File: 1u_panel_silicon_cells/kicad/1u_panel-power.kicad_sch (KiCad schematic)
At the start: 70 parts, among them J1 MMS-104-01-[F/L]-SH, Q1 DMP3050LVT-7, Q2 DMP2240UDM-7, U10 TPS63060DSCR, U12 LTC4412, U3 LT1618EMSTRPBF, U4 INA226

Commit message: Updated all PN/DS/DPN/MPN/etc. for silicon solar module components
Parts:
- C12: DPN 490-12379-1-ND -> 490-10516-2-ND; MPN GRT21BR61C106KE01L -> GRM21BR71A106KA73L
- C14, C18: DPN 587-4332-1-ND -> 490-GRM188Z71C475KE21JTR-ND; MFR Taiyo -> Murata; MPN EMK107BBJ475KAHT -> GRM188Z71C475KE21J
- C2: DPN 587-5957-1-ND -> 490-4781-2-ND; MFR Taiyo -> Murata; MPN UMK107B7103KAHT -> GCM188R72A103KA37D
- C21, C6, C7, C8: DPN 1276-6985-1-ND -> 490-5798-2-ND; MFR Kemet -> Murata; MPN CL10B104KB85PND -> GCJ188R71H104KA12D
- C22: DPN 490-12317-1-ND -> 490-8011-2-ND; MPN GRT188R61C106KE13D -> GCM1885G1H100JA16D
- L1: DPN 445-VLS3010CX-1R5M-1CT-ND -> 490-14149-2-ND; MFR TDK -> Murata
- R1: DPN A129720CT-ND -> YAG4574TR-ND; MFR TE -> Yaego; MPN CRGCQ0603F470K -> RT0603BRD07560KL
- R17: DPN 541-100MAHTR-ND -> P19308TR-ND; MFR Vishay -> Panasonic; MPN CRCW0603100MJPEAHR -> ERJ-6DSFR10V
- R18, R19, R6, R7: DPN RNCP0603FTD10K0CT-ND -> RR08P100KDCT-ND; MFR Stackpole -> Susumu; MPN RNCP0603FTD10K0 -> RR0816P-104-D
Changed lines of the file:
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@@
 			)
 		)
-		(property "DPN" "1276-6985-1-ND"
+		(property "DPN" "490-5798-2-ND"
 			(at 118.11 77.47 0)
 			(effects
@@
 			)
 		)
-		(property "MFR" "Kemet"
+		(property "MFR" "Murata"
 			(at 118.11 77.47 0)
 			(effects
@@
 			)
 		)
-		(property "MPN" "CL10B104KB85PND"
+		(property "MPN" "GCJ188R71H104KA12D"
 			(at 118.11 77.47 0)
 			(effects
@@
 			)
 		)
-		(property "DPN" "587-5957-1-ND"
+		(property "DPN" "490-4781-2-ND"
 			(at 223.52 105.41 0)
 			(effects
@@
 			)
 		)
-		(property "MFR" "Taiyo"
+		(property "MFR" "Murata"
 			(at 223.52 105.41 0)
 			(effects
@@
 			)
 		)
-		(property "MPN" "UMK107B7103KAHT"
+		(property "MPN" "GCM188R72A103KA37D"
 			(at 223.52 105.41 0)
 			(effects
@@
 			)
 		)
-		(property "DPN" "445-VLS3010CX-1R5M-1CT-ND"
+		(property "DPN" "490-14149-2-ND"
 			(at 182.88 205.74 0)
 			(effects
@@
 			)
 		)
-		(property "MFR" "TDK"
+		(property "MFR" "Murata"
 			(at 182.88 205.74 0)
 			(effects
@@
 			)
 		)
-		(property "DPN" "587-4332-1-ND"
+		(property "DPN" "490-GRM188Z71C475KE21JTR-ND"
 			(at 238.76 64.77 0)
 			(effects
@@
 			)
 		)
-		(property "MFR" "Taiyo"
+		(property "MFR" "Murata"
 			(at 238.76 64.77 0)
 			(effects
@@
 			)
 		)
-		(property "MPN" "EMK107BBJ475KAHT"
+		(property "MPN" "GRM188Z71C475KE21J"
 			(at 238.76 64.77 0)
 			(effects
@@
 			)
 		)
-		(property "DPN" "A129720CT-ND"
+		(property "DPN" "YAG4574TR-ND"
 			(at 219.71 198.12 0)
 			(effects
@@
 			)
 		)
-		(property "MFR" "TE"
+		(property "MFR" "Yaego"
 			(at 219.71 198.12 0)
 			(effects
@@
 			)
 		)
-		(property "MPN" "CRGCQ0603F470K"
+		(property "MPN" "RT0603BRD07560KL"
 			(at 219.71 198.12 0)
 			(effects
@@
 			)
 		)
-		(property "DPN" "RNCP0603FTD10K0CT-ND"
+		(property "DPN" "RR08P100KDCT-ND"
 			(at 162.56 100.33 0)
 			(effects
@@
 			)
 		)
-		(property "MFR" "Stackpole"
+		(property "MFR" "Susumu"
 			(at 162.56 100.33 0)
 			(effects
@@
 			)
 		)
-		(property "MPN" "RNCP0603FTD10K0"
+		(property "MPN" "RR0816P-104-D"
 			(at 162.56 100.33 0)
 			(effects
@@
 			)
 		)
-		(property "DPN" "RNCP0603FTD10K0CT-ND"
+		(property "DPN" "RR08P100KDCT-ND"
 			(at 177.8 104.14 0)
 			(effects
@@
 			)
 		)
-		(property "MFR" "Stackpole"
+		(property "MFR" "Susumu"
 			(at 177.8 104.14 0)
 			(effects
@@
 			)
 		)
-		(property "MPN" "RNCP0603FTD10K0"
+		(property "MPN" "RR0816P-104-D"
 			(at 177.8 104.14 0)
 			(effects
@@
 			)
 		)
-		(property "DPN" "RNCP0603FTD10K0CT-ND"
+		(property "DPN" "RR08P100KDCT-ND"
 			(at 290.83 86.36 0)
 			(effects
@@
 			)
 		)
-		(property "MFR" "Stackpole"
+		(property "MFR" "Susumu"
 			(at 290.83 86.36 0)
 			(effects
@@
 			)
 		)
-		(property "MPN" "RNCP0603FTD10K0"
+		(property "MPN" "RR0816P-104-D"
 			(at 290.83 86.36 0)
 			(effects
@@
 			)
 		)
-		(property "DPN" "1276-6985-1-ND"
+		(property "DPN" "490-5798-2-ND"
 			(at 208.28 222.25 0)
 			(effects
@@
 			)
 		)
-		(property "MFR" "Kemet"
+		(property "MFR" "Murata"
 			(at 208.28 222.25 0)
 			(effects
@@
 			)
 		)
-		(property "MPN" "CL10B104KB85PND"
+		(property "MPN" "GCJ188R71H104KA12D"
 			(at 208.28 222.25 0)
 			(effects
@@
 			)
 		)
-		(property "DPN" "1276-6985-1-ND"
+		(property "DPN" "490-5798-2-ND"
 			(at 303.53 66.04 0)
 			(effects
@@
 			)
 		)
-		(property "MFR" "Kemet"
+		(property "MFR" "Murata"
 			(at 303.53 66.04 0)
 			(effects
@@
 			)
 		)
-		(property "MPN" "CL10B104KB85PND"
+		(property "MPN" "GCJ188R71H104KA12D"
 			(at 303.53 66.04 0)
 			(effects
@@
 			)
 		)
-		(property "DPN" "1276-6985-1-ND"
+		(property "DPN" "490-5798-2-ND"
 			(at 58.42 66.04 0)
 			(effects
@@
 			)
 		)
-		(property "MFR" "Kemet"
+		(property "MFR" "Murata"
 			(at 58.42 66.04 0)
 			(effects
@@
 			)
 		)
-		(property "MPN" "CL10B104KB85PND"
+		(property "MPN" "GCJ188R71H104KA12D"
 			(at 58.42 66.04 0)
 			(effects
@@
 			)
 		)
-		(property "DPN" "587-4332-1-ND"
+		(property "DPN" "490-GRM188Z71C475KE21JTR-ND"
 			(at 162.56 64.77 0)
 			(effects
@@
 			)
 		)
-		(property "MFR" "Taiyo"
+		(property "MFR" "Murata"
 			(at 162.56 64.77 0)
 			(effects
@@
 			)
 		)
-		(property "MPN" "EMK107BBJ475KAHT"
+		(property "MPN" "GRM188Z71C475KE21J"
 			(at 162.56 64.77 0)
 			(effects
@@
 			)
 		)
-		(property "DPN" "541-100MAHTR-ND"
+		(property "DPN" "P19308TR-ND"
 			(at 187.96 59.69 0)
 			(effects
@@
 			)
 		)
-		(property "MFR" "Vishay"
+		(property "MFR" "Panasonic"
 			(at 187.96 59.69 0)
 			(effects
@@
 			)
 		)
-		(property "MPN" "CRCW0603100MJPEAHR"
+		(property "MPN" "ERJ-6DSFR10V"
 			(at 187.96 59.69 0)
 			(effects
@@
 			)
 		)
-		(property "DPN" "490-12317-1-ND"
+		(property "DPN" "490-8011-2-ND"
 			(at 226.06 207.01 0)
 			(effects
@@
 			)
 		)
-		(property "MPN" "GRT188R61C106KE13D"
+		(property "MPN" "GCM1885G1H100JA16D"
 			(at 226.06 207.01 0)
 			(effects
@@
 			)
 		)
-		(property "DPN" "490-12379-1-ND"
+		(property "DPN" "490-10516-2-ND"
 			(at 137.16 196.85 0)
 			(effects
@@
 			)
 		)
-		(property "MPN" "GRT21BR61C106KE01L"
+		(property "MPN" "GRM21BR71A106KA73L"
 			(at 137.16 196.85 0)
 			(effects
@@
 			)
 		)
-		(property "DPN" "RNCP0603FTD10K0CT-ND"
+		(property "DPN" "RR08P100KDCT-ND"
 			(at 165.1 195.58 0)
 			(effects
@@
 			)
 		)
-		(property "MFR" "Stackpole"
+		(property "MFR" "Susumu"
 			(at 165.1 195.58 0)
 			(effects
@@
 			)
 		)
-		(property "MPN" "RNCP0603FTD10K0"
+		(property "MPN" "RR0816P-104-D"
 			(at 165.1 195.58 0)
 			(effects

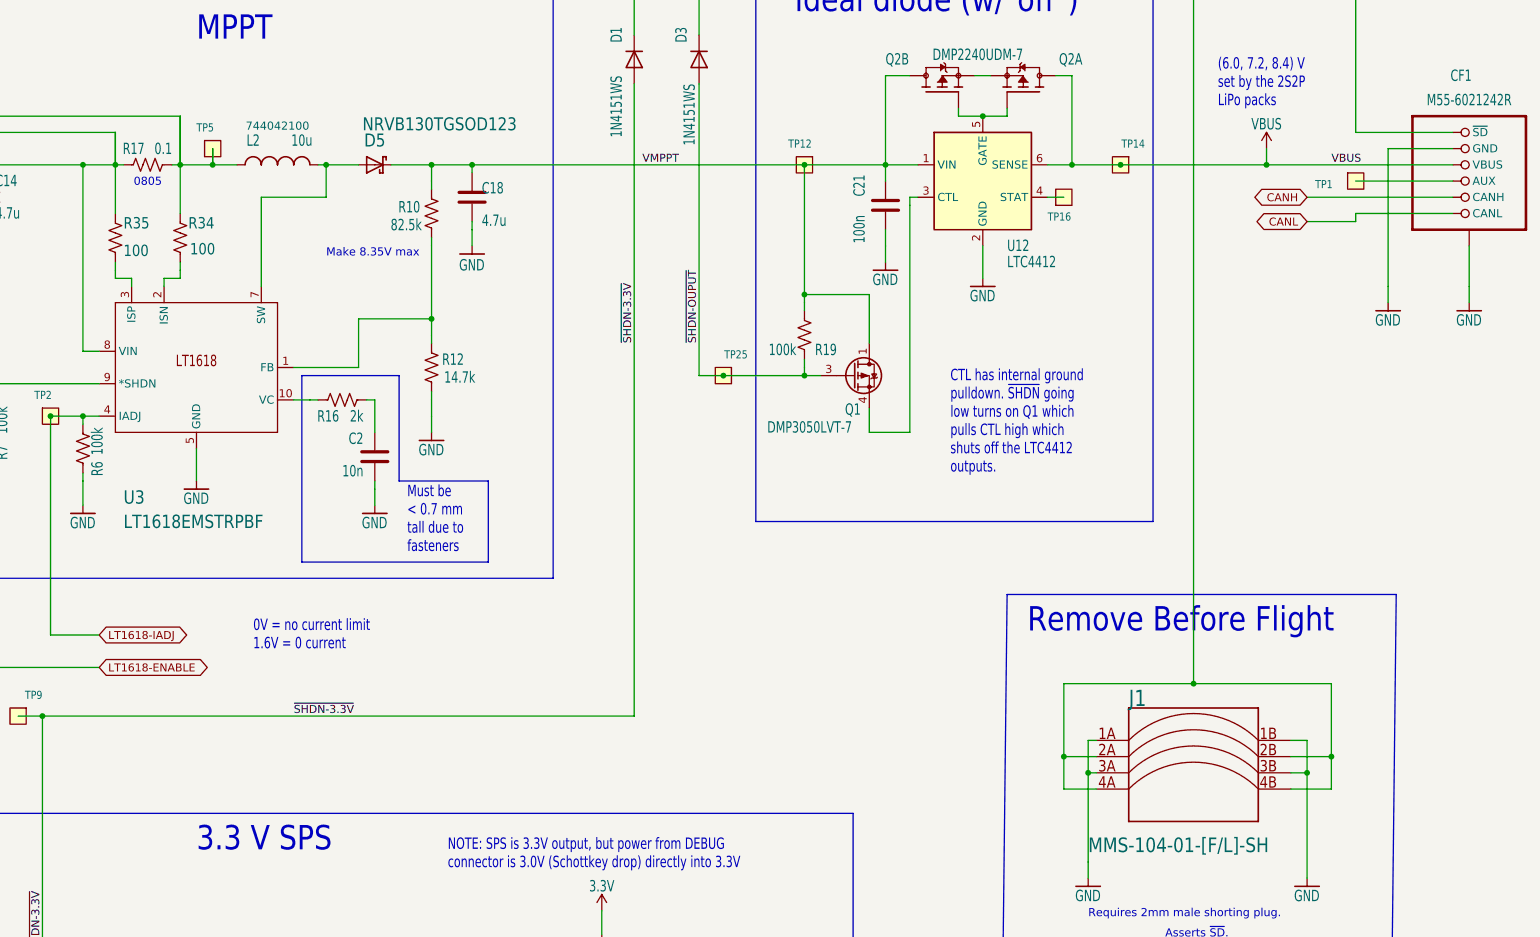
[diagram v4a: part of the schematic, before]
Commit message: finished DR changes for silicon solar module
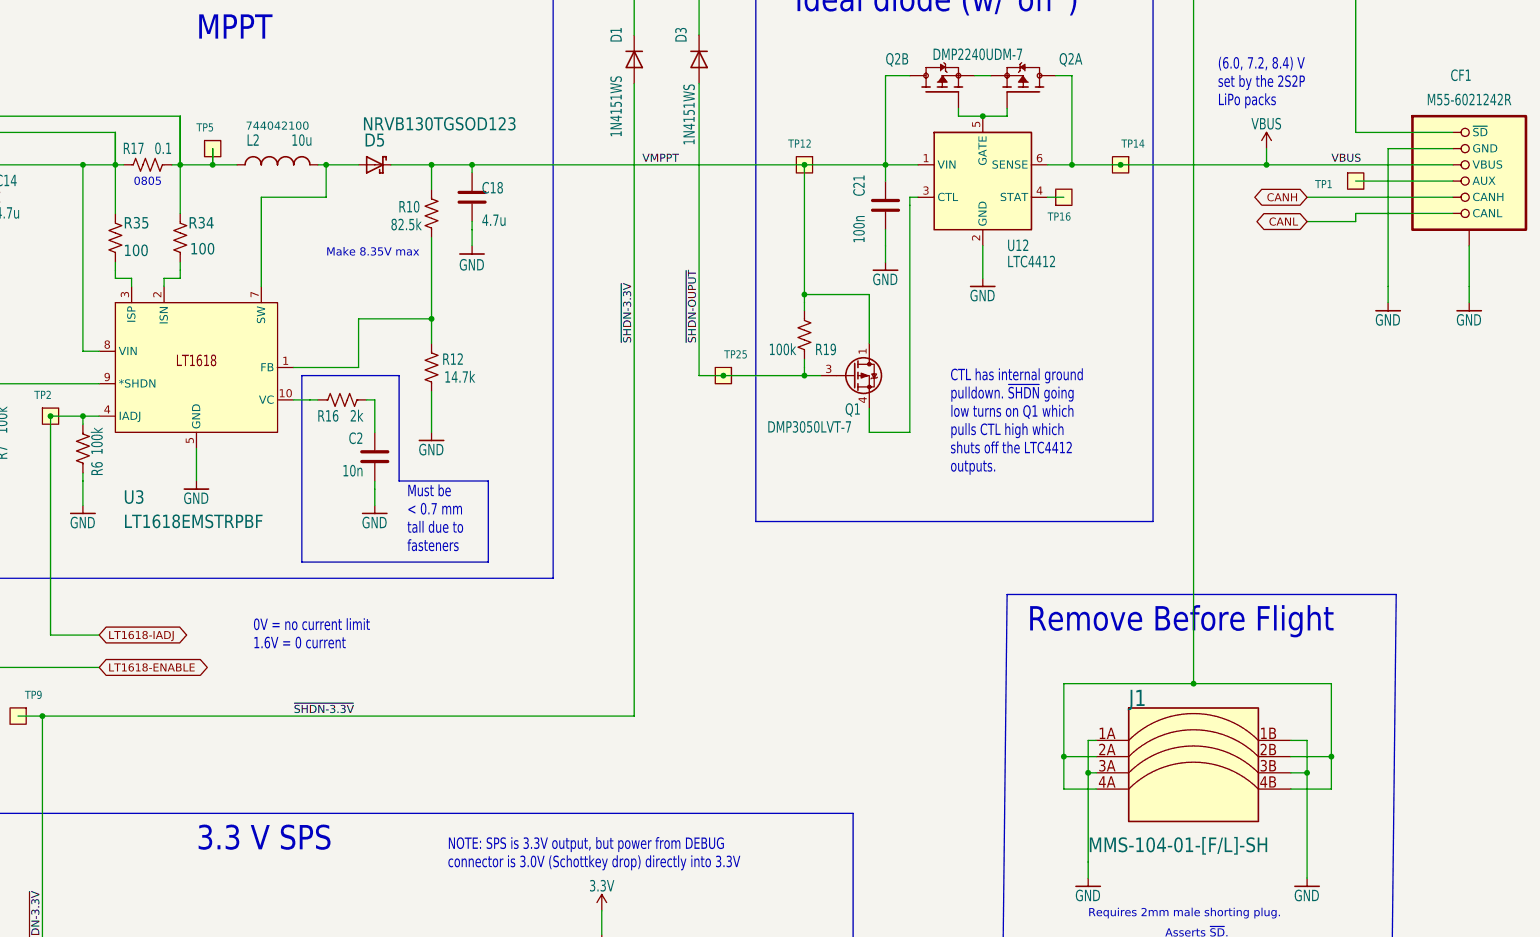
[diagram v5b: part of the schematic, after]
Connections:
- net GND: now also CF1.P$1 (SHIELD), CF1.P$2 (SHIELD), CF1.P$3 (SHIELD), CF1.P$4 (SHIELD); no longer CF1.SH1 (SHIELD), CF1.SH2 (SHIELD), CF1.SH3 (SHIELD), CF1.SH4 (SHIELD)
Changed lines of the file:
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@@
 		(pin "9"
 		)
-		(pin "SH1"
+		(pin "P$1"
 		)
-		(pin "SH4"
+		(pin "P$4"
 		)
-		(pin "SH2"
+		(pin "P$3"
 		)
-		(pin "SH3"
+		(pin "P$2"
 		)
 		(instances

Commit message: final changes for silicon solar module
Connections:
- no-connect marks 0 -> 1
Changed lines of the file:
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@@
 		(color 0 0 0 0)
 	)
+	(no_connect
+		(at 180.34 86.36)
+	)
 	(polyline
 		(pts
@@
 	(wire
 		(pts
-			(xy 180.34 88.9) (xy 177.8 88.9)
+			(xy 180.34 90.17) (xy 177.8 90.17)
 		)
 		(stroke
@@
 	(wire
 		(pts
-			(xy 177.8 88.9) (xy 177.8 59.69)
+			(xy 177.8 90.17) (xy 177.8 59.69)
 		)
 		(stroke
@@
 		(pin "9"
 		)
+		(pin "6"
+		)
 		(instances

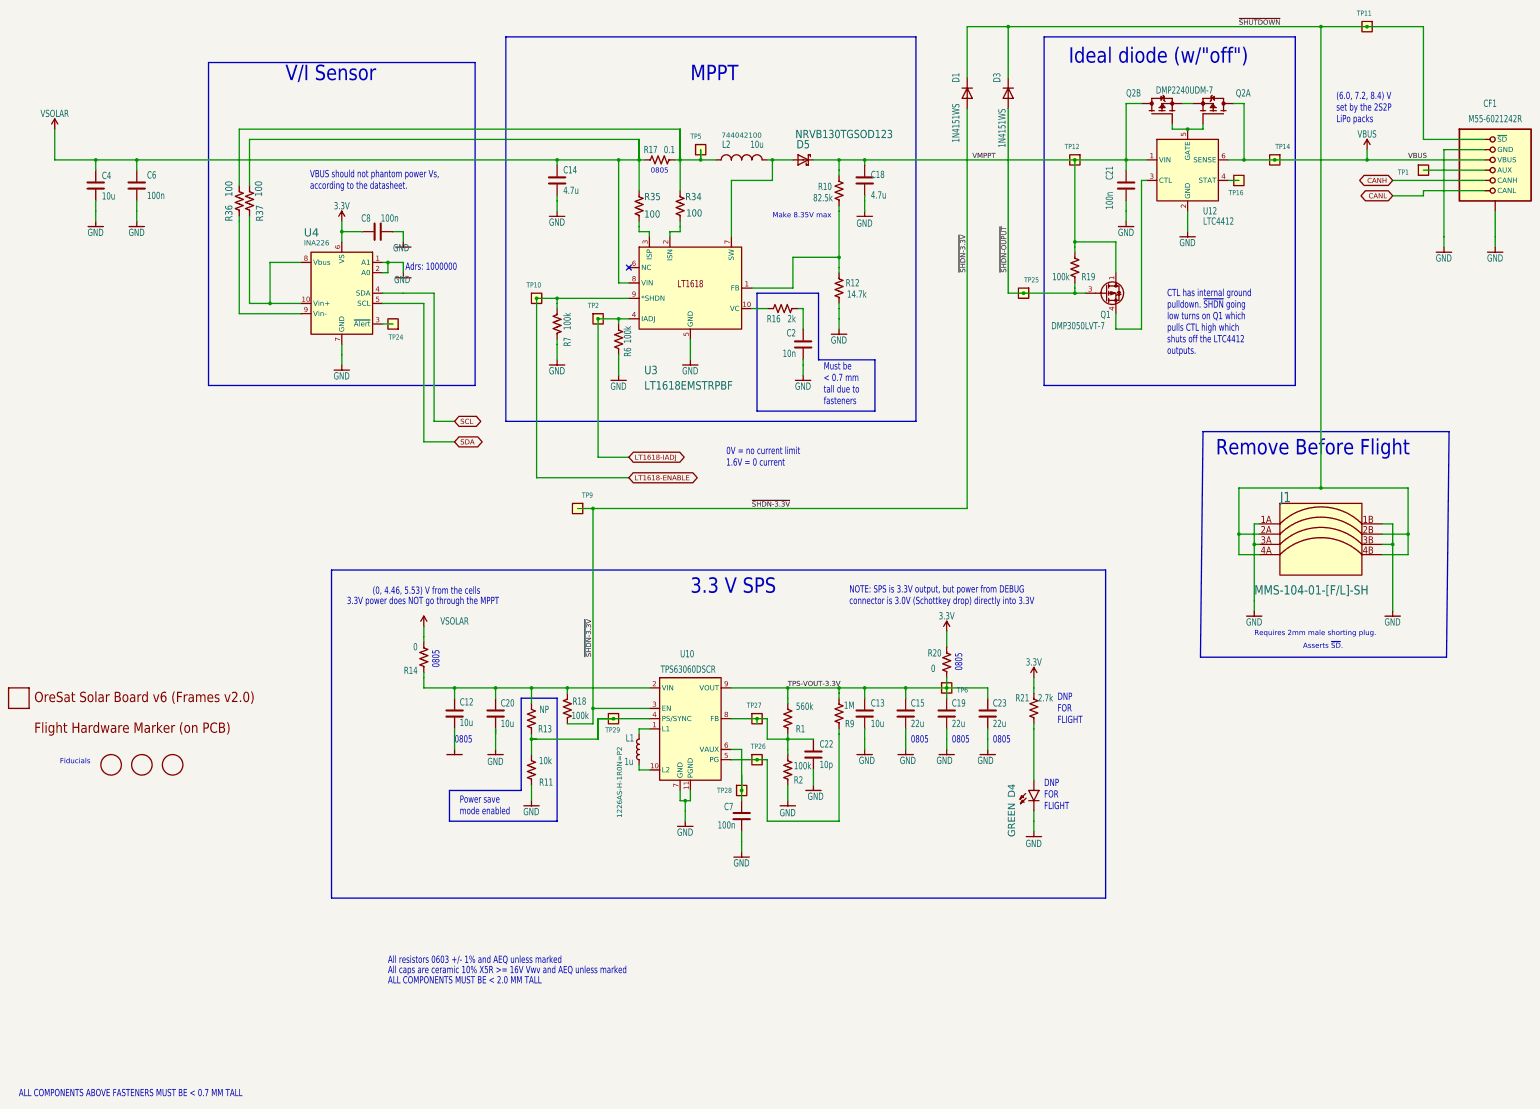
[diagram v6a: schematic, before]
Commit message: Polish on Jack's final design. Swapped out rectangles for zones on multiple layers, cleaned up a lot of small layout bits, fixed some mechanical crashes with screw heads, fixed up the silk screen, and added 3D models.
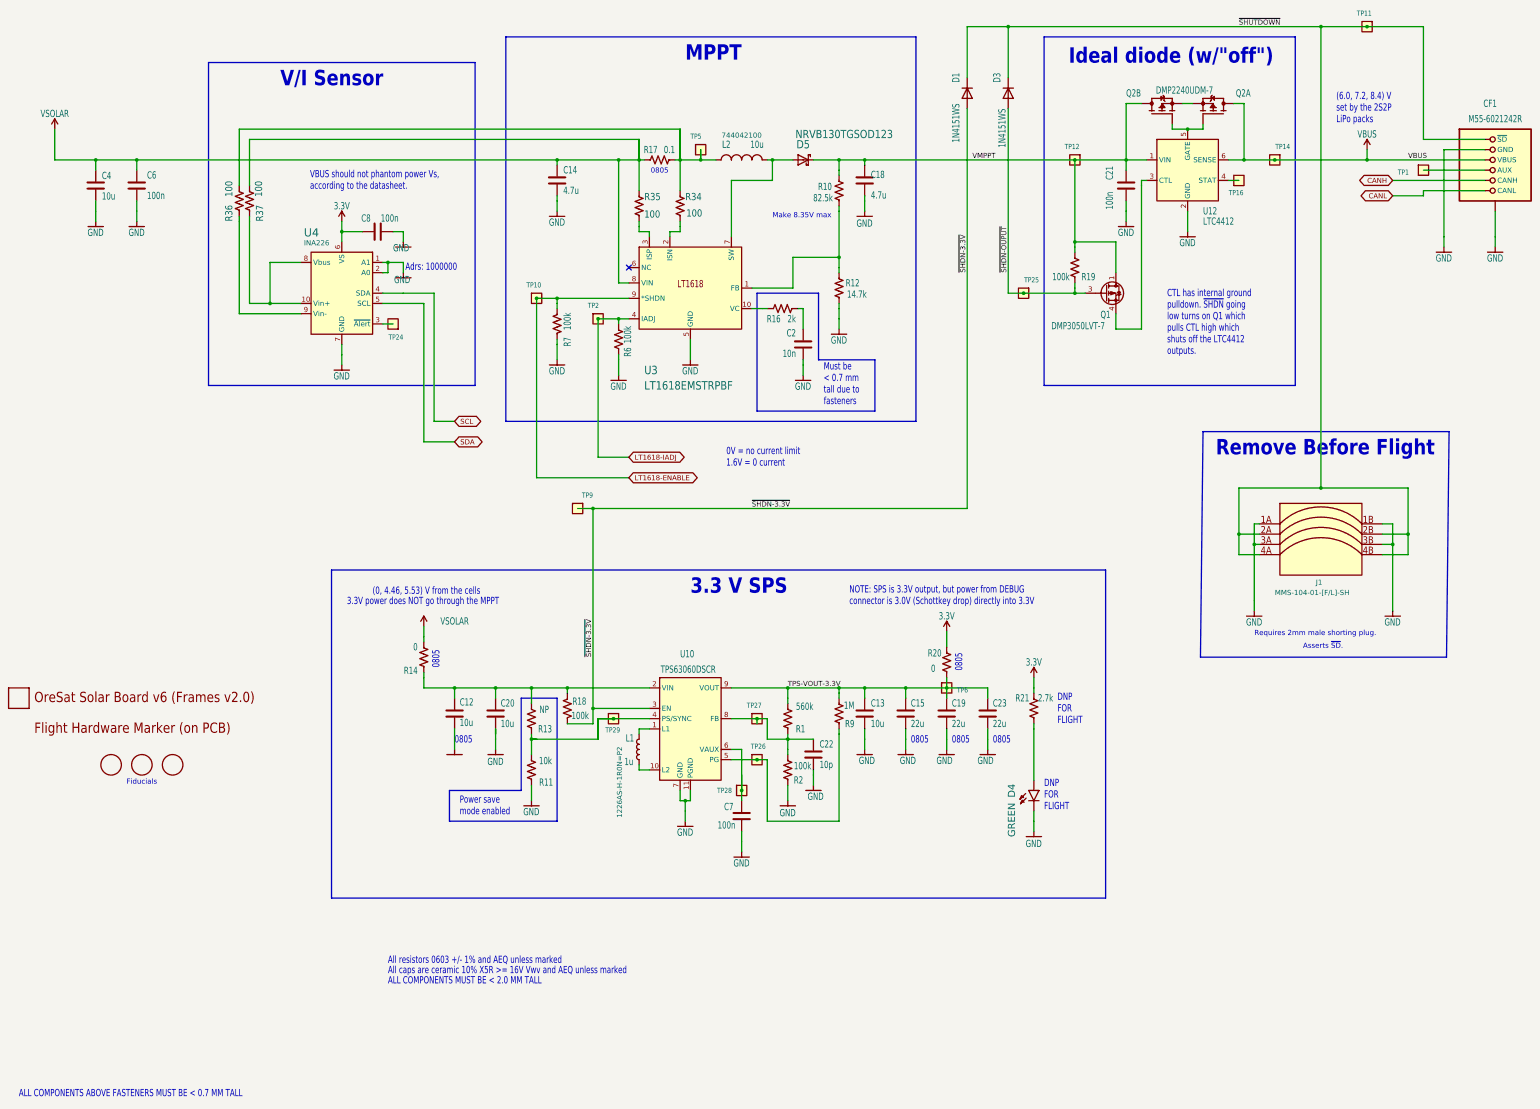
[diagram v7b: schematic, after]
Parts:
- U$2, U$3, U$4: now left out of the parts list
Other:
- title: OreSat Silicon Solar Module (for Frame 2.0) -> OreSat Solar Module - Silicon Cells
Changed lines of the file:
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@@
 	(paper "USLedger")
 	(title_block
-		(title "OreSat Silicon Solar Module (for Frame 2.0)")
-		(date "2024-08-18")
+		(title "OreSat Solar Module - Silicon Cells")
+		(date "2024-09-22")
 		(rev "1.0")
 	)
@@
 			(font
 				(size 3.81 3.2385)
+				(thickness 0.6477)
+				(bold yes)
 			)
 			(justify left bottom)
@@
 	(text "MPPT"
 		(exclude_from_sim no)
-		(at 195.58 40.64 0)
+		(at 194.31 35.56 0)
 		(effects
 			(font
 				(size 3.81 3.2385)
+				(thickness 0.6477)
+				(bold yes)
 			)
 			(justify left bottom)
@@
 			(font
 				(size 3.81 3.2385)
+				(thickness 0.6477)
+				(bold yes)
 			)
 			(justify left bottom)
@@
 	(text "Fiducials"
 		(exclude_from_sim no)
-		(at 39.37 209.55 0)
+		(at 55.88 214.63 0)
 		(effects
 			(font
@@
 			(font
 				(size 3.81 3.2385)
+				(thickness 0.6477)
+				(bold yes)
 			)
 			(justify left bottom)
@@
 	(text "V/I Sensor"
 		(exclude_from_sim no)
-		(at 95.25 40.64 0)
+		(at 93.98 41.91 0)
 		(effects
 			(font
 				(size 3.81 3.2385)
+				(thickness 0.6477)
+				(bold yes)
 			)
 			(justify left bottom)
@@
 		(at 52.07 209.55 0)
 		(unit 1)
-		(exclude_from_sim no)
-		(in_bom yes)
+		(exclude_from_sim yes)
+		(in_bom no)
 		(on_board yes)
 		(dnp no)
@@
 		(at 67.31 209.55 0)
 		(unit 1)
-		(exclude_from_sim no)
-		(in_bom yes)
+		(exclude_from_sim yes)
+		(in_bom no)
 		(on_board yes)
 		(dnp no)
@@
 		(dnp no)
 		(property "Reference" "J1"
-			(at 341.63 144.78 0)
+			(at 350.52 165.1 0)
 			(effects
 				(font
-					(size 2.54 2.159)
+					(size 1.27 1.27)
 				)
 				(justify left bottom)
@@
 		)
 		(property "Value" "MMS-104-01-[F/L]-SH"
-			(at 335.28 167.64 0)
+			(at 340.36 167.64 0)
 			(effects
 				(font
-					(size 2.286 1.9431)
+					(size 1.27 1.27)
 				)
 				(justify left bottom)
@@
 		(at 59.69 209.55 0)
 		(unit 1)
-		(exclude_from_sim no)
-		(in_bom yes)
+		(exclude_from_sim yes)
+		(in_bom no)
 		(on_board yes)
 		(dnp no)
